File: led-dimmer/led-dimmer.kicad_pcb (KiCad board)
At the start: 2 copper layers, 34 x 34 mm, 22 parts, among them J1 Screw_Terminal_01x02, J2 Screw_Terminal_01x02, Q1 IRLML6344, U1 LM555xM

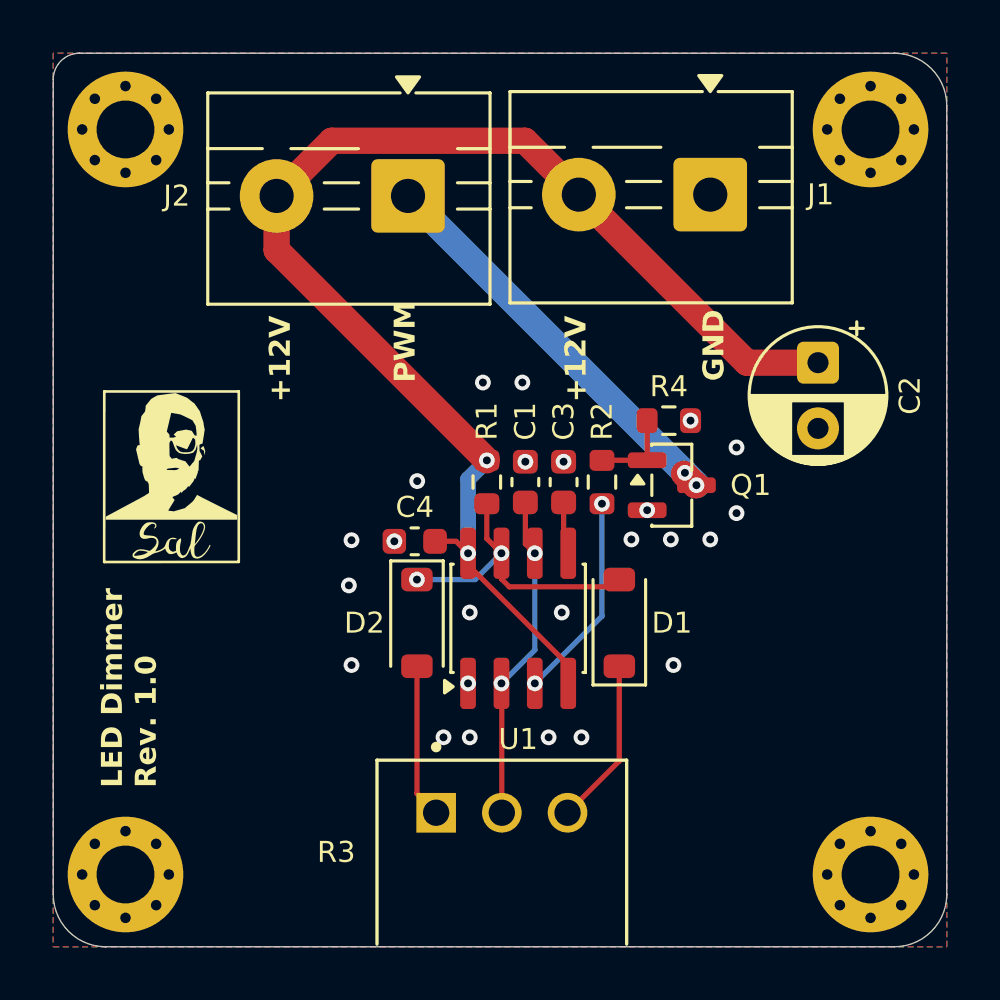
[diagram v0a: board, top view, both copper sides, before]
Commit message: Updated LED Schematic and PCB
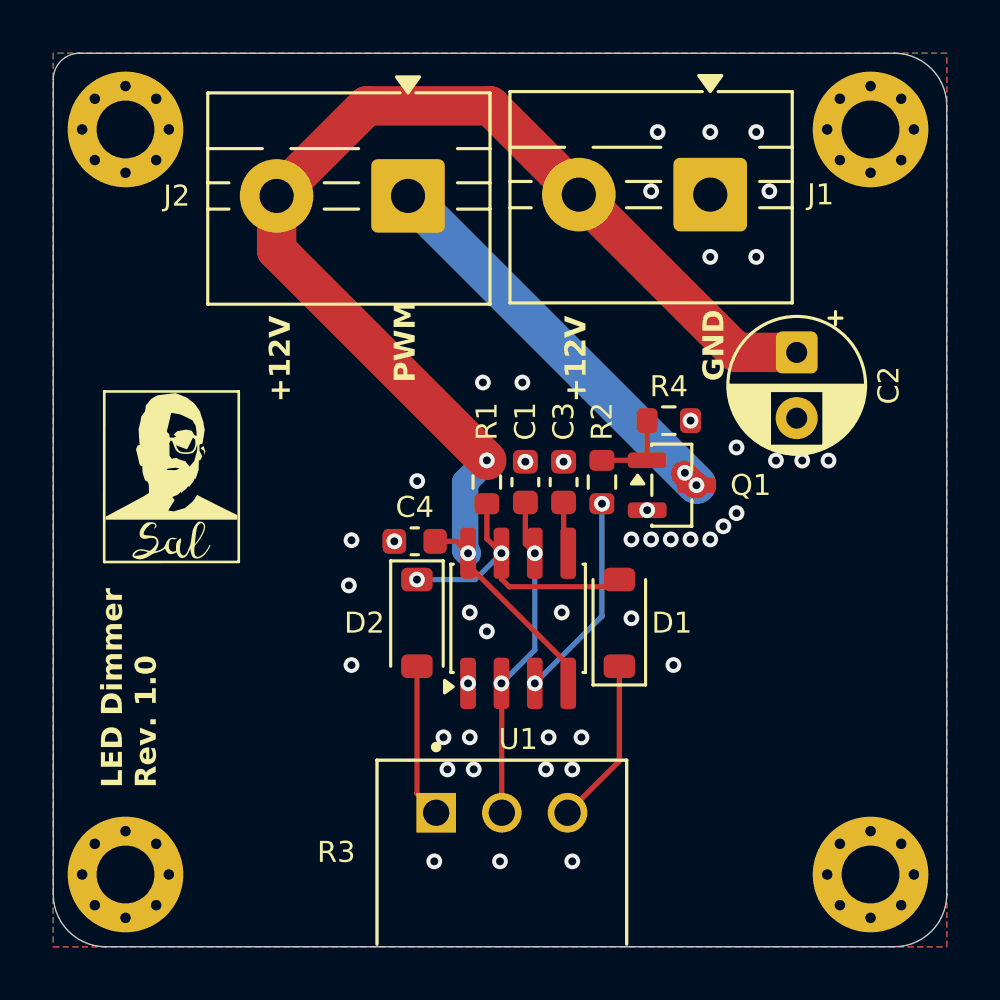
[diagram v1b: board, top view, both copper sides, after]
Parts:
- moved REF** 1.47 mm to (92.0, 114.0)
- moved C2 0.90 mm to (96.3, 107.4)
- moved REF** 0.50 mm to (82.4, 113.6)
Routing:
- net GND: vias 24 -> 46
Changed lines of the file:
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@@
 	(title_block
 		(title "LED Dimmer PCB")
-		(date "2026-06-28")
+		(date "2026-07-20")
 		(rev "1.0")
 	)
@@
 	(footprint "Capacitor_THT:CP_Radial_D5.0mm_P2.50mm"
 		(layer "F.Cu")
-		(at 97.1 107.774888 -90)
+		(at 96.29 107.384888 -90)
 		(descr "CP, Radial series, Radial, pin pitch=2.50mm, diameter=5mm, height=7mm, Electrolytic Capacitor")
 		(tags "CP Radial series Radial pin pitch 2.50mm diameter 5mm height 7mm Electrolytic Capacitor")
@@
 	(footprint "Symbol:KiCad-Logo2_5mm_SilkScreen"
 		(layer "B.Cu")
-		(at 81.9 113.6 180)
+		(at 82.4 113.6 180)
 		(descr "KiCad Logo")
 		(tags "Logo KiCad")
@@
 	(footprint "Symbol:WEEE-Logo_4.2x6mm_SilkScreen"
 		(layer "B.Cu")
-		(at 93.465 113.955 180)
+		(at 92 113.955 180)
 		(descr "Waste Electrical and Electronic Equipment Directive https://eur-lex.europa.eu/legal-content/EN/TXT/PDF/?uri=CELEX:32012L0019#page=29")
 		(tags "Logo WEEE")
@@
 	)
 	(segment
-		(start 92.475 112.405)
-		(end 92.475 112.4375)
-		(width 1)
+		(start 81.5 101.43)
+		(end 92.475 112.405)
+		(width 1.5)
 		(layer "B.Cu")
 		(net "LED_PWM")
 	)
 	(segment
-		(start 92.035 111.965)
-		(end 92.475 112.405)
-		(width 1)
-		(layer "B.Cu")
-		(net "LED_PWM")
+		(start 88 101.38)
+		(end 84.62 98)
+		(width 1.5)
+		(layer "F.Cu")
+		(net "+12V")
 	)
 	(segment
-		(start 81.5 101.43)
-		(end 92.035 111.965)
-		(width 1)
-		(layer "B.Cu")
-		(net "LED_PWM")
+		(start 83.785 115.0275)
+		(end 83.33 114.5725)
+		(width 0.2)
+		(layer "F.Cu")
+		(net "+12V")
 	)
 	(segment
-		(start 78.6 99.33)
-		(end 76.5 101.43)
-		(width 1)
+		(start 94.004888 107.384888)
+		(end 96.29 107.384888)
+		(width 1.5)
 		(layer "F.Cu")
 		(net "+12V")
 	)
 	(segment
-		(start 94.394888 107.774888)
-		(end 97.1 107.774888)
-		(width 1)
+		(start 79.93 98)
+		(end 76.5 101.43)
+		(width 1.5)
 		(layer "F.Cu")
 		(net "+12V")
 	)
 	(segment
-		(start 76.5 103.4925)
-		(end 84.5 111.4925)
-		(width 1)
+		(start 83.785 115.0275)
+		(end 83.785 115.465)
+		(width 0.2)
 		(layer "F.Cu")
 		(net "+12V")
@@
 		(start 76.5 101.43)
 		(end 76.5 103.4925)
-		(width 1)
+		(width 1.5)
 		(layer "F.Cu")
 		(net "+12V")
@@
 	(segment
 		(start 88 101.38)
-		(end 94.394888 107.774888)
-		(width 1)
+		(end 94.004888 107.384888)
+		(width 1.5)
 		(layer "F.Cu")
 		(net "+12V")
 	)
 	(segment
-		(start 82.53 114.5725)
-		(end 83.33 114.5725)
-		(width 0.2)
+		(start 76.5 103.4925)
+		(end 84.5 111.4925)
+		(width 1.5)
 		(layer "F.Cu")
 		(net "+12V")
 	)
 	(segment
-		(start 83.33 114.5725)
-		(end 83.785 115.0275)
+		(start 82.53 114.5725)
+		(end 82.4 114.5725)
 		(width 0.2)
 		(layer "F.Cu")
@@
 	)
 	(segment
-		(start 82.53 114.5725)
-		(end 82.4 114.5725)
-		(width 0.2)
+		(start 84.62 98)
+		(end 79.93 98)
+		(width 1.5)
 		(layer "F.Cu")
 		(net "+12V")
@@
 	)
 	(segment
-		(start 88 101.38)
-		(end 85.95 99.33)
-		(width 1)
-		(layer "F.Cu")
-		(net "+12V")
-	)
-	(segment
-		(start 85.95 99.33)
-		(end 78.6 99.33)
-		(width 1)
-		(layer "F.Cu")
-		(net "+12V")
-	)
-	(segment
-		(start 83.785 115.0275)
-		(end 83.785 115.465)
+		(start 83.785 115.465)
+		(end 87.595 119.275)
 		(width 0.2)
 		(layer "F.Cu")
@@
 	)
 	(segment
-		(start 83.785 115.465)
-		(end 87.595 119.275)
+		(start 83.33 114.5725)
+		(end 82.53 114.5725)
 		(width 0.2)
 		(layer "F.Cu")
@@
 	(segment
 		(start 83.785 115.0275)
-		(end 83.785 112.2075)
-		(width 0.6)
+		(end 83.677538 114.920038)
+		(width 1)
+		(layer "B.Cu")
+		(net "+12V")
+	)
+	(segment
+		(start 83.677538 114.920038)
+		(end 83.677538 112.314962)
+		(width 1)
 		(layer "B.Cu")
 		(net "+12V")
 	)
 	(segment
-		(start 83.785 112.2075)
+		(start 83.677538 112.314962)
 		(end 84.5 111.4925)
-		(width 0.6)
+		(width 1)
 		(layer "B.Cu")
 		(net "+12V")
@@
 	)
 	(via
+		(at 92.25 114.5)
+		(size 0.6)
+		(drill 0.3)
+		(layers "F.Cu" "B.Cu")
+		(free yes)
+		(net "GND")
+	)
+	(via
+		(at 93 99)
+		(size 0.6)
+		(drill 0.3)
+		(layers "F.Cu" "B.Cu")
+		(free yes)
+		(net "GND")
+	)
+	(via
+		(at 87.75 126.75)
+		(size 0.6)
+		(drill 0.3)
+		(layers "F.Cu" "B.Cu")
+		(free yes)
+		(net "GND")
+	)
+	(via
 		(at 88.1 122.03)
 		(size 0.6)
@@
 	)
 	(via
+		(at 95.5 111.5)
+		(size 0.6)
+		(drill 0.3)
+		(layers "F.Cu" "B.Cu")
+		(free yes)
+		(net "GND")
+	)
+	(via
+		(at 90.75 101.25)
+		(size 0.6)
+		(drill 0.3)
+		(layers "F.Cu" "B.Cu")
+		(free yes)
+		(net "GND")
+	)
+	(via
 		(at 80.98 114.5725)
 		(size 0.6)
@@
 	)
 	(via
+		(at 93.5 114)
+		(size 0.6)
+		(drill 0.3)
+		(layers "F.Cu" "B.Cu")
+		(free yes)
+		(net "GND")
+	)
+	(via
 		(at 79.35 119.28)
 		(size 0.6)
@@
 	)
 	(via
+		(at 96.5 111.5)
+		(size 0.6)
+		(drill 0.3)
+		(layers "F.Cu" "B.Cu")
+		(free yes)
+		(net "GND")
+	)
+	(via
+		(at 93 103.75)
+		(size 0.6)
+		(drill 0.3)
+		(layers "F.Cu" "B.Cu")
+		(free yes)
+		(net "GND")
+	)
+	(via
 		(at 93 114.5)
 		(size 0.6)
@@
 	)
 	(via
+		(at 90 117.5)
+		(size 0.6)
+		(drill 0.3)
+		(layers "F.Cu" "B.Cu")
+		(free yes)
+		(net "GND")
+	)
+	(via
 		(at 94 111)
 		(size 0.6)
@@
 	)
 	(via
+		(at 95.25 101.25)
+		(size 0.6)
+		(drill 0.3)
+		(layers "F.Cu" "B.Cu")
+		(free yes)
+		(net "GND")
+	)
+	(via
 		(at 92.25 109.98)
 		(size 0.6)
@@
 	)
 	(via
+		(at 83 123.25)
+		(size 0.6)
+		(drill 0.3)
+		(layers "F.Cu" "B.Cu")
+		(free yes)
+		(net "GND")
+	)
+	(via
+		(at 97.5 111.5)
+		(size 0.6)
+		(drill 0.3)
+		(layers "F.Cu" "B.Cu")
+		(free yes)
+		(net "GND")
+	)
+	(via
 		(at 91.6 119.28)
 		(size 0.6)
@@
 	)
 	(via
+		(at 90.75 114.5)
+		(size 0.6)
+		(drill 0.3)
+		(layers "F.Cu" "B.Cu")
+		(free yes)
+		(net "GND")
+	)
+	(via
 		(at 87.42 111.5425)
 		(size 0.6)
@@
 	)
 	(via
+		(at 91 99)
+		(size 0.6)
+		(drill 0.3)
+		(layers "F.Cu" "B.Cu")
+		(free yes)
+		(net "GND")
+	)
+	(via
 		(at 83.785 119.9775)
 		(size 0.6)
@@
 	)
 	(via
+		(at 94.75 103.75)
+		(size 0.6)
+		(drill 0.3)
+		(layers "F.Cu" "B.Cu")
+		(free yes)
+		(net "GND")
+	)
+	(via
 		(at 94 113.5)
 		(size 0.6)
@@
 	)
 	(via
+		(at 84 123.25)
+		(size 0.6)
+		(drill 0.3)
+		(layers "F.Cu" "B.Cu")
+		(free yes)
+		(net "GND")
+	)
+	(via
 		(at 90.6 113.3875)
 		(size 0.6)
@@
 	)
 	(via
+		(at 84.5 118)
+		(size 0.6)
+		(drill 0.3)
+		(layers "F.Cu" "B.Cu")
+		(free yes)
+		(net "GND")
+	)
+	(via
+		(at 82.5 126.75)
+		(size 0.6)
+		(drill 0.3)
+		(layers "F.Cu" "B.Cu")
+		(free yes)
+		(net "GND")
+	)
+	(via
 		(at 85.965 111.5425)
 		(size 0.6)
@@
 	)
 	(via
+		(at 94.75 99)
+		(size 0.6)
+		(drill 0.3)
+		(layers "F.Cu" "B.Cu")
+		(free yes)
+		(net "GND")
+	)
+	(via
+		(at 85 126.75)
+		(size 0.6)
+		(drill 0.3)
+		(layers "F.Cu" "B.Cu")
+		(free yes)
+		(net "GND")
+	)
+	(via
 		(at 84.35 108.53)
 		(size 0.6)
@@
 	)
 	(via
+		(at 86.75 123.25)
+		(size 0.6)
+		(drill 0.3)
+		(layers "F.Cu" "B.Cu")
+		(free yes)
+		(net "GND")
+	)
+	(via
 		(at 79.25 116.25)
 		(size 0.6)
 		(drill 0.3)
+		(layers "F.Cu" "B.Cu")
+		(free yes)
+		(net "GND")
+	)
+	(via
+		(at 87.75 123.25)
+		(size 0.6)
+		(drill 0.3)

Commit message: Updated output connectors and slimmed LED Dimmer PCB
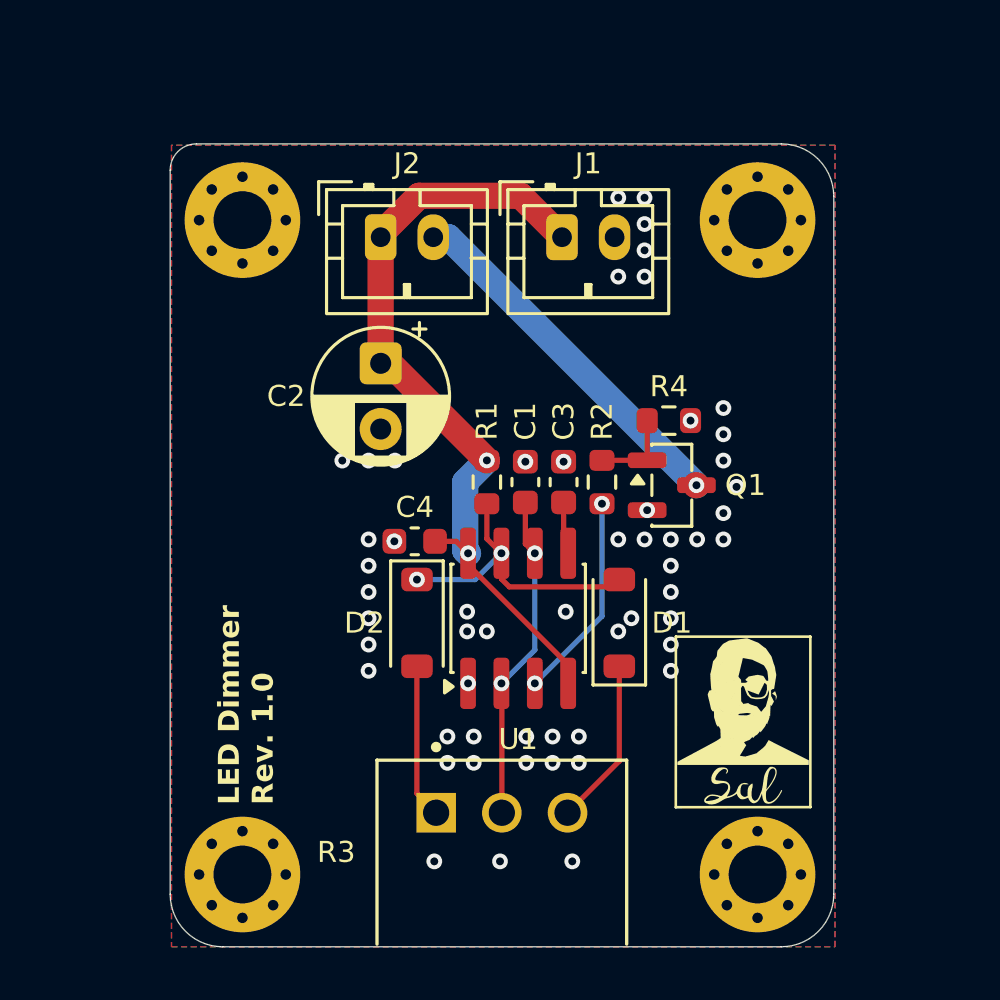
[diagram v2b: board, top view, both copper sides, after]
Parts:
- added G***: LOGO, footprints:SalSig, B.Cu at (76.0, 123.8)
- added G***: LOGO, footprints:SalLogo, B.Cu at (76.0, 120.5)
- J1, J2: value Screw_Terminal_01x02 -> Conn_01x02_Pin; footprint TerminalBlock:TerminalBlock_MaiXu_MX126-5.0-02P_1x02_P5.00mm -> Connector_JST:JST_PH_B2B-PH-K_1x02_P2.00mm_Vertical
- moved G*** 23.7 mm to (94.2, 120.6)
- moved G*** 23.7 mm to (94.2, 123.9)
- moved C2 15.8 mm to (80.5, 107.8)
- moved J1 5.87 mm to (87.4, 103.0), turned to 0 degrees
- moved REF** 5.63 mm to (75.2, 102.3)
- moved REF** 5.51 mm to (94.8, 102.3)
- moved REF** 4.45 mm to (75.2, 127.2)
- moved REF** 4.30 mm to (94.8, 127.2)
- moved J2 1.88 mm to (80.5, 103.0), turned to 0 degrees
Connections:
- J1 pad 1: GND -> +12V
- J1 pad 2: +12V -> GND
- J2 pad 1: LED_PWM -> +12V
- J2 pad 2: +12V -> LED_PWM
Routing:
- net +12V: track 50.5 -> 30.7 mm
- net LED_PWM: track 16.2 -> 14.0 mm, vias 2 -> 1
- net GND: vias 46 -> 57
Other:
- board size 34 x 34 mm -> 25.2 x 30.5 mm
- board text removed: "+12V"
- board text removed: "GND"
- board text removed: "PWM"

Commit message: Update LED dimmer PCB for revised components
- Switch power and LED connections to JST B2B-XH-A connectors
- Update bulk capacitor to 470uF
- Change NE555 to DIP-8 package
- Increase PCB size and revise component placement/routing
- Update schematic reference designators
- Refresh README component and design documentation
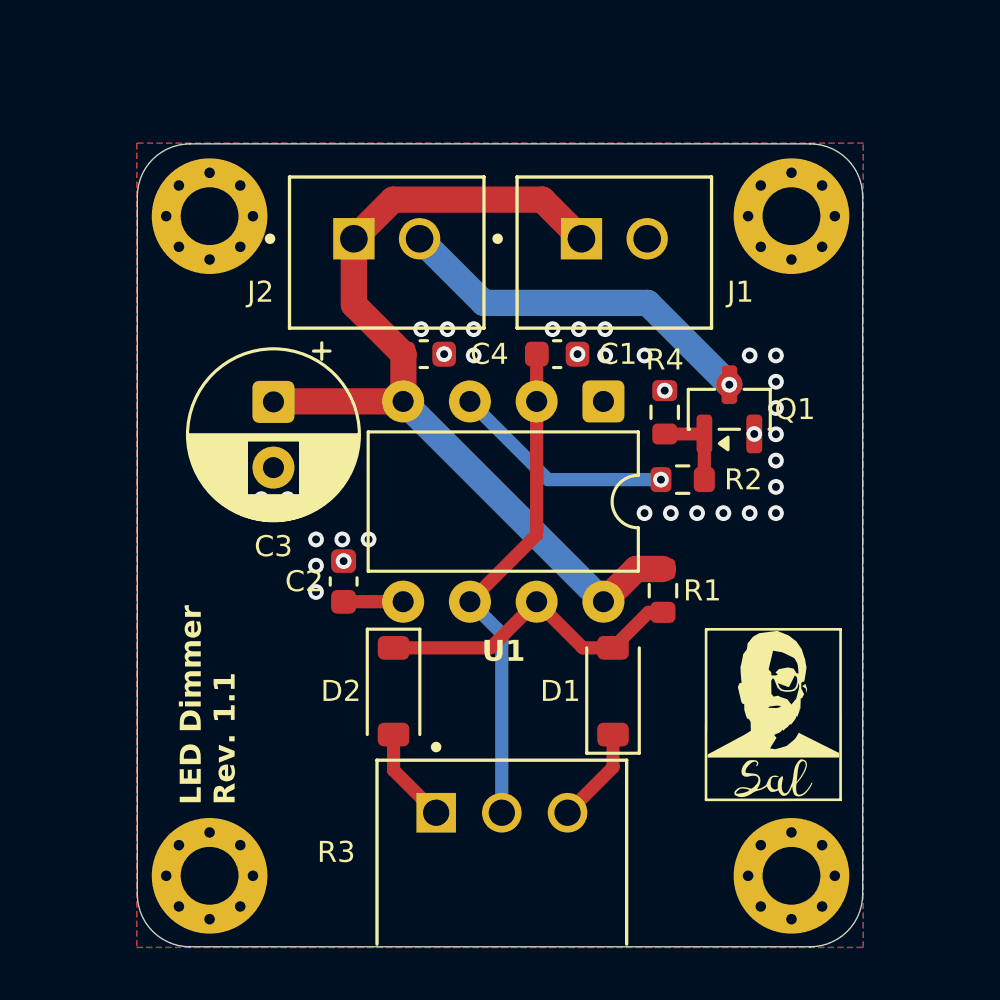
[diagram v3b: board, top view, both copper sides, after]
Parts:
- C3: renamed from C2; value 100u -> 470u; footprint Capacitor_THT:CP_Radial_D5.0mm_P2.50mm -> Capacitor_THT:CP_Radial_D6.3mm_P2.50mm
- J1, J2: footprint Connector_JST:JST_PH_B2B-PH-K_1x02_P2.00mm_Vertical -> footprints:JST_B2B-XH-A
- U1: value LM555xM -> NE555P; footprint Package_SO:SOIC-8_3.9x4.9mm_P1.27mm -> Package_DIP:DIP-8_W7.62mm
- moved C2 9.18 mm to (79.0, 116.1)
- moved U1 8.87 mm to (88.9, 109.2), turned to -90 degrees
- moved R1 7.87 mm to (91.2, 116.5)
- moved C4 7.13 mm to (82.1, 107.5), turned to 0 degrees
- moved C1 5.02 mm to (87.2, 107.5), turned to 0 degrees
- moved C3 4.34 mm to (76.4, 109.3)
- moved Q1 3.62 mm to (93.7, 109.5), turned to 90 degrees
- moved R2 3.07 mm to (92.0, 112.2), turned to 180 degrees
- moved D2 2.75 mm to (81.0, 120.3)
- moved D1 2.61 mm to (89.3, 120.3)
- moved J1 2.07 mm to (89.3, 103.6), turned to 180 degrees
- moved G*** 1.51 mm to (74.5, 123.6)
- moved G*** 1.51 mm to (74.5, 120.3)
- moved REF** 1.30 mm to (83.5, 113.0)
- moved REF** 1.30 mm to (93.1, 113.3)
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- renumbered C3 to C2
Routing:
- net TIMING: track 12.6 -> 19.0 mm, vias 2 -> 0
- net +12V: track 30.7 -> 35.4 mm, vias 2 -> 0
- net Net-(D1-K): track 6.39 -> 3.69 mm
- net Net-(D2-A): track 5.87 -> 3.65 mm
- net DISCHARGE: track 11.4 -> 12.3 mm, vias 2 -> 0
- net Net-(U1-OUT): track 7.89 -> 8.50 mm, vias 2 -> 1
- net GND: vias 57 -> 37
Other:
- board size 25.2 x 30.5 mm -> 27.6 x 30.5 mm
- board text added: "LED Dimmer Rev. 1.1"
- board text removed: "LED Dimmer Rev. 1.0"
